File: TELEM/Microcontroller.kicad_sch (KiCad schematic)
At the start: 17 parts, among them J4 Conn_01x02_Pin, M3 MountingHole, M3_1 MountingHole, U2 ESP32-DEVKIT-C, U3 TJA1050T/CM,118

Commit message: PDB_Schematic mostly updated
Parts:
- added M4: MountingHole, MountingHole:MountingHole_3.2mm_M3, symbol Mechanical:MountingHole
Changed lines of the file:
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@@
+	)
+	(symbol
+		(lib_id "Mechanical:MountingHole")
+		(at 201.93 82.55 0)
+		(unit 1)
+		(body_style 1)
+		(exclude_from_sim no)
+		(in_bom no)
+		(on_board yes)
+		(in_pos_files yes)
+		(dnp no)
+		(fields_autoplaced yes)
+		(property "Reference" "M4"
+			(at 204.47 81.2799 0)
+			(show_name no)
+			(do_not_autoplace no)
+			(effects
+				(font
+					(size 1.27 1.27)
+				)
+				(justify left)
+			)
+		)
+		(property "Value" "MountingHole"
+			(at 204.47 83.8199 0)
+			(show_name no)
+			(do_not_autoplace no)
+			(effects
+				(font
+					(size 1.27 1.27)
+				)
+				(justify left)
+			)
+		)
+		(property "Footprint" "MountingHole:MountingHole_3.2mm_M3"
+			(at 201.93 82.55 0)
+			(hide yes)
+			(show_name no)
+			(do_not_autoplace no)
+			(effects
+				(font
+					(size 1.27 1.27)
+				)
+			)
+		)
+		(property "Datasheet" ""
+			(at 201.93 82.55 0)
+			(hide yes)
+			(show_name no)
+			(do_not_autoplace no)
+			(effects
+				(font
+					(size 1.27 1.27)
+				)
+			)
+		)
+		(property "Description" "Mounting Hole without connection"
+			(at 201.93 82.55 0)
+			(hide yes)
+			(show_name no)
+			(do_not_autoplace no)
+			(effects
+				(font
+					(size 1.27 1.27)
+				)
+			)
+		)
+		(instances
+			(project "Microcontroller"
+				(path "/c58806c5-432f-4c41-8983-8e5fd30a3703"
+					(reference "M4")
+					(unit 1)
+				)
+			)
+		)
 	)
 	(symbol

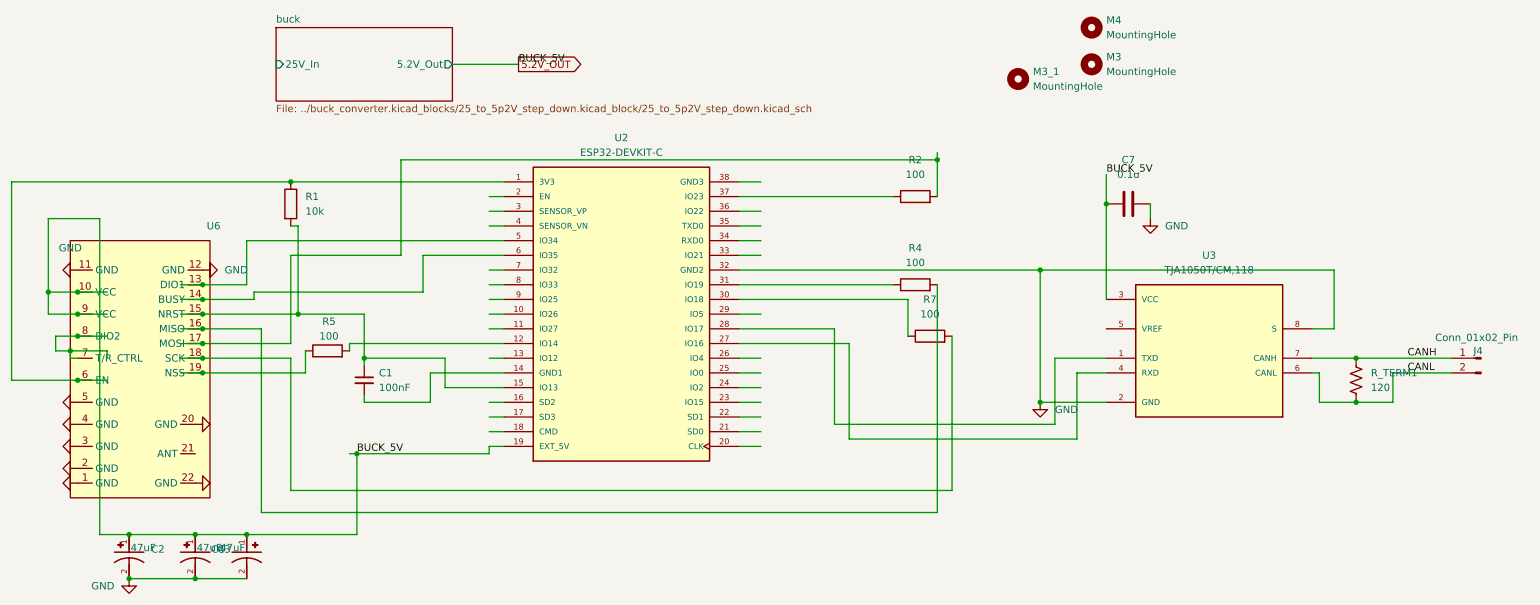
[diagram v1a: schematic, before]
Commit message: sry forgot to push, waiting on PCB shipping atm. Notes: split power distribution into two boards, one for the main 25V distribution, and another for 12V stuff. Also updated CAN transciever. the previous one was a 5V logic one (same logic as its power), and would have fried our ESPs data pins
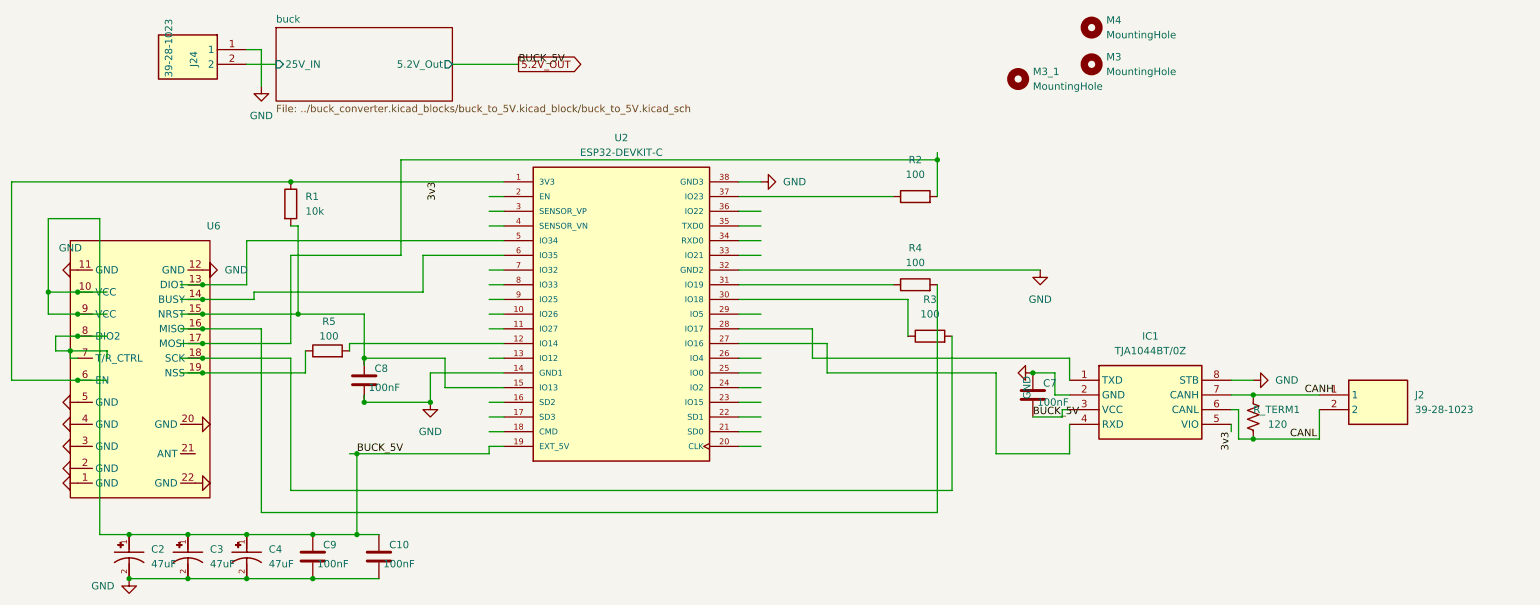
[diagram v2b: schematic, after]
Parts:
- removed C1: 100nF, Capacitor_SMD:C_1206_3216Metric_Pad1.33x1.80mm_HandSolder, symbol Device:C_Small
- removed J4: Conn_01x02_Pin, PROVE-footprints:TE_1877285-2, symbol Connector:Conn_01x02_Pin
- removed U3: TJA1050T/CM,118, Package_SO:SOIC-8_3.9x4.9mm_P1.27mm, symbol PROVE:TJA1050T/CM,118
- added C10, C8, C9: 100nF, Capacitor_SMD:C_0805_2012Metric_Pad1.18x1.45mm_HandSolder, symbol PROVE:1206B104K500CT
- added IC1: TJA1044BT/0Z, PROVE-footprints:SOIC127P600X175-8N, symbol PROVE_Symbols:TJA1044BT_0Z
- added J2, J24: 39-28-1023, PROVE-footprints:39-28-1023, symbol PROVE_Symbols:39-28-1023
- C2, C3, C4: Purchase Link https://www.mouser.com/en/ProductDetail/KEMET/T520B476M010A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 -> https://www.mouser.com/en/ProductDetail/KEMET/T598B476M010A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; Specs Cap: 47 µF VDC: 10 V ESR: 35 mΩ -> Cap: 47 µF VDC: 10 V
- C7: value 0.1u -> 100nF; footprint Capacitor_SMD:C_1206_3216Metric_Pad1.33x1.80mm_HandSolder -> Capacitor_SMD:C_0805_2012Metric_Pad1.18x1.45mm_HandSolder; Purchase Link (none) -> https://www.mouser.com/en/ProductDetail/KEMET/C0805X104K1RA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; Specs (none) -> 100 nF, 100 V, X7R, ±10%
- R_TERM1: footprint Resistor_SMD:R_1206_3216Metric_Pad1.30x1.75mm_HandSolder -> Resistor_SMD:R_0805_2012Metric_Pad1.20x1.40mm_HandSolder; Purchase Link (none) -> https://www.mouser.com/en/ProductDetail/Vishay/CRCW0805120R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; Specs (none) -> 120 Ω, ±1%, AEC-Q200,
- renumbered R7 to R3
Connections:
- net 5.2V_OUT: now also C7.1, C10.2, C9.2, IC1.3 (VCC); no longer C7.2
- net CANH: now also IC1.7 (CANH), J2.1
- net CANL: now also IC1.6 (CANL), J2.2
- net GND: now also C7.2, U2.14 (GND1), U2.38 (GND3), C10.1, C8.1, C9.1, IC1.2 (GND), IC1.8 (STB), J24.1; no longer C7.1
- net 3v3: now reaches R1.1, U2.1 (3V3), U6.6 (EN)
- net 3v3: now also IC1.5 (VIO)
- net at R1.2, U2.15 (IO13), U6.15 (NRST): now also C8.2
- net at U2.27 (IO16): now also IC1.4 (RXD)
- net at U2.28 (IO17): now also IC1.1 (TXD)
- new net buck/25V_IN: J24.2
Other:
- sheet buck: file ../buck_converter.kicad_blocks/25_to_5p2V_step_down.kicad_block/25_to_5p2V_step_down.kicad_sch -> ../buck_converter.kicad_blocks/buck_to_5V.kicad_block/buck_to_5V.kicad_sch
- sheet buck ports: added 25V_IN; removed 25V_In
